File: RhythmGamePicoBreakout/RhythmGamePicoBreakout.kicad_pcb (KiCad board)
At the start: 2 copper layers, 80 x 54 mm, 71 parts, among them J1 BUTTON0, J10 BUTTON9, J11 BUTTON10, J12 QE1, J13 QE2, J14 Conn_01x02_Pin, J15 RGB1, J16 RGB2, J17 USB Header, J18 USB_C_Receptacle_USB2.0, J19 Conn_01x03, J2 BUTTON1, J20 PS2 Header, J21 Conn_01x02_Pin, J3 BUTTON2, J4 BUTTON3, J5 BUTTON4, J6 BUTTON5, J7 BUTTON6, J8 BUTTON7, J9 BUTTON8, Q1 LSI1012LT1G, Q10 LSI1012LT1G, Q11 LSI1012LT1G, Q2 LSI1012LT1G, Q3 LSI1012LT1G, Q4 LSI1012LT1G, Q5 LSI1012LT1G, Q6 LSI1012LT1G, Q7 LSI1012LT1G, Q8 LSI1012LT1G, Q9 LSI1012LT1G, U1 RP2040, U2 SRV05-4, U3 W25Q128JVS, U4 XC6206PxxxMR, U5 SN74HCT125D, U6 LM7805_TO220, Y1 Crystal_GND24

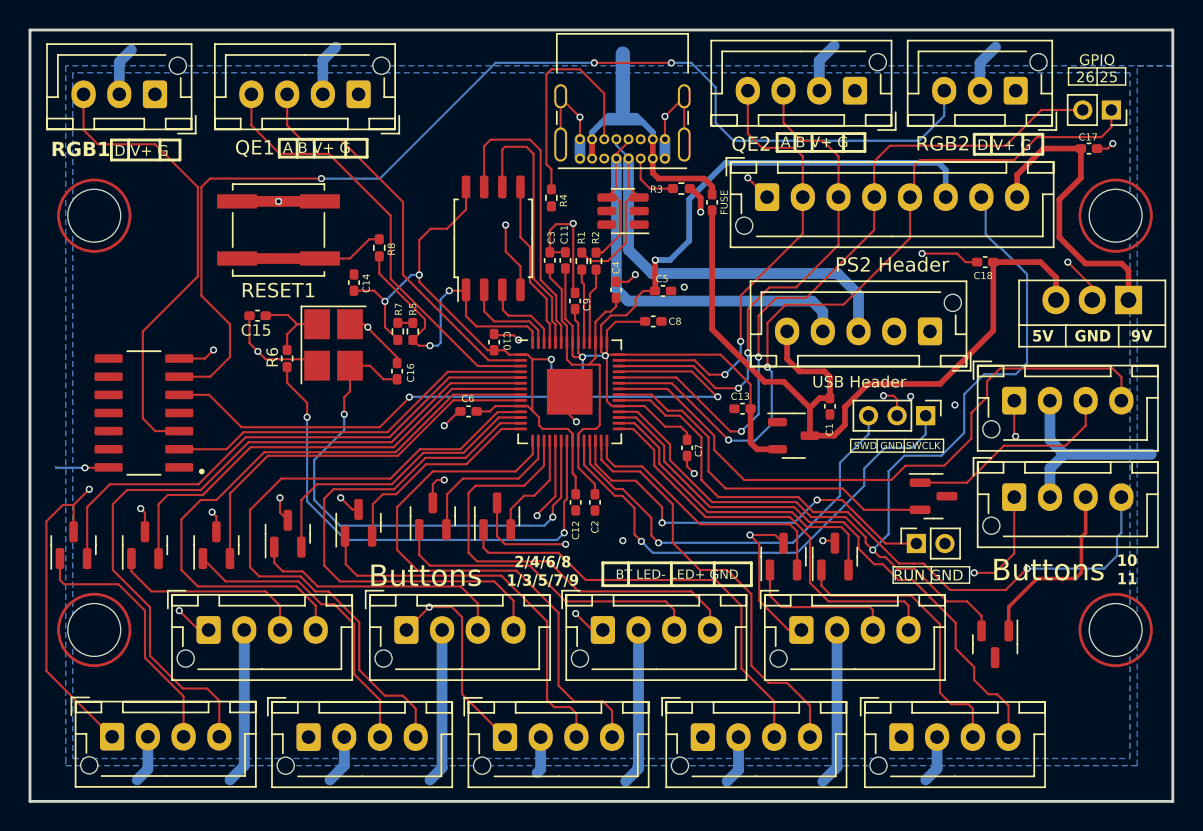
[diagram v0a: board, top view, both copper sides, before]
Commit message: Updated schematics and completely redone tracing
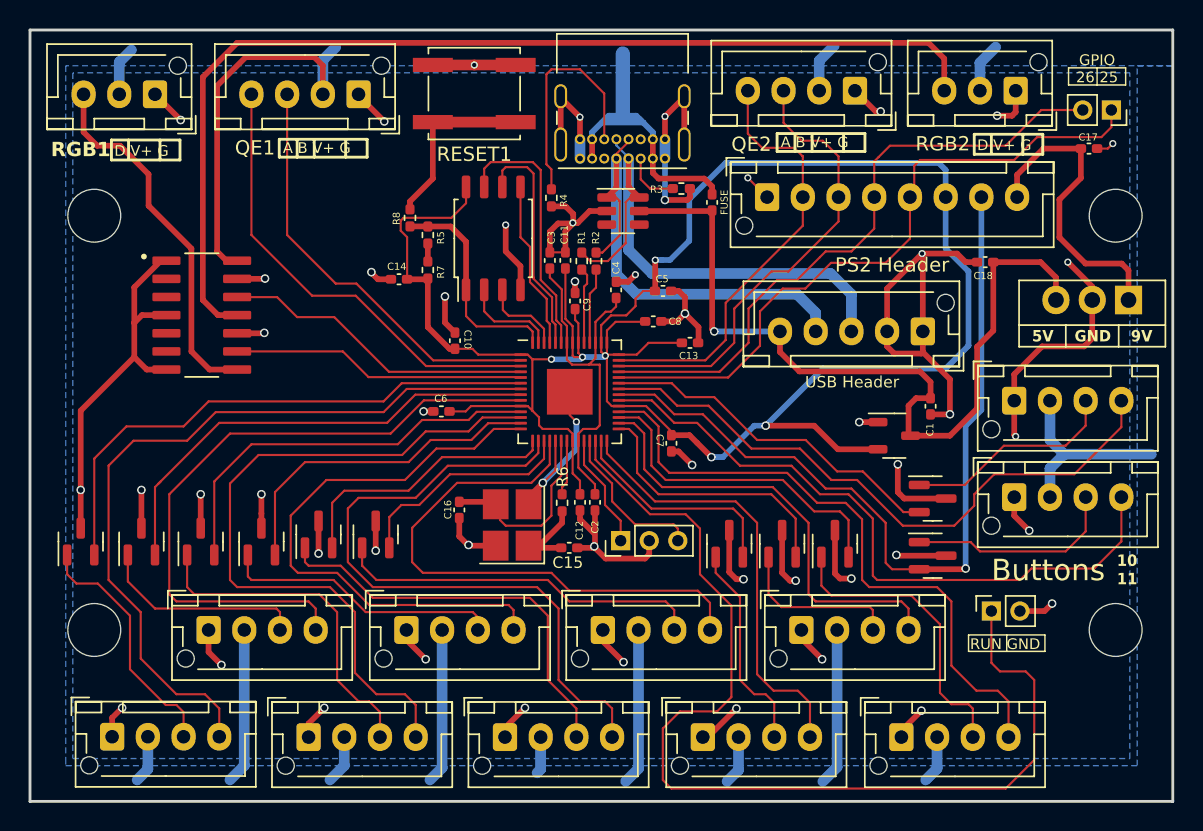
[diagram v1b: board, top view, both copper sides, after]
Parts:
- J19: value Conn_01x03 -> DEBUG
- moved C15 27.2 mm to (103.2, 161.8), turned to 180 degrees
- moved J19 23.1 mm to (106.8, 161.2), turned to 90 degrees
- moved R6 21.7 mm to (102.8, 158.6), turned to 90 degrees
- moved Y1 17.7 mm to (99.2, 160.2), turned to 90 degrees
- moved RESET1 16.7 mm to (96.6, 129.9)
- moved Q7 16.4 mm to (114.5, 161.5)
- moved C16 10.6 mm to (95.5, 159.1), turned to 90 degrees
- moved U5 7.96 mm to (77.5, 145.5), turned to 0 degrees
- moved Q11 7.59 mm to (128.7, 162.3), turned to 0 degrees
- moved J21 7.06 mm to (132.8, 166.2)
- moved C1 7.04 mm to (128.5, 151.8)
- moved U4 7.04 mm to (126.0, 153.9)
- moved R5 6.83 mm to (93.3, 139.9), turned to 90 degrees
- moved C13 5.90 mm to (111.7, 147.4), turned to 0 degrees
- moved R7 4.78 mm to (93.3, 142.3)
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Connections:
- U1 pad 11: /BT2 -> /LED2
- U1 pad 12: /LED3 -> /BT2
- U1 pad 13: /BT3 -> /LED3
- U1 pad 14: /LED4 -> /BT3
- U1 pad 15: /BT4 -> /LED4
- U1 pad 16: /LED5 -> /BT4
- U1 pad 17: /BT5 -> /LED5
- U1 pad 18: /LED6 -> /BT5
- U1 pad 27: /BT6 -> /LED6
- U1 pad 28: /LED7 -> /BT6
- U1 pad 29: /BT7 -> /LED7
- U1 pad 30: /LED8 -> /BT7
- U1 pad 31: /BT8 -> /LED8
- U1 pad 32: /LED10 -> /BT8
- U1 pad 35: /LED9 -> /LED10
- U1 pad 37: /GP25 -> /LED9
- U1 pad 38: /GP26 -> /GP25
- U1 pad 39: /RGBIn2 -> /GP26
- U1 pad 4: /RGBIn1 -> /RGBIn2
- U1 pad 5: /LED0 -> /RGBIn1
- U1 pad 6: /BT0 -> /LED0
- U1 pad 7: /LED1 -> /BT0
- U1 pad 8: /BT1 -> /LED1
- U1 pad 9: /LED2 -> /BT1
- U2 pad 1: unconnected-(U2-IO1-Pad1) -> USB_DM
- U2 pad 3: USB_DP -> unconnected-(U2-IO2-Pad3)
- U2 pad 4: USB_DM -> unconnected-(U2-IO3-Pad4)
- U2 pad 6: unconnected-(U2-IO4-Pad6) -> USB_DP
- U5 pad 11: unconnected-(U5-4Y-Pad11) -> /RGB2
- U5 pad 12: unconnected-(U5-4A-Pad12) -> /RGBIn2
- U5 pad 2: /RGBIn1 -> unconnected-(U5-1A-Pad2)
- U5 pad 3: /RGB1 -> unconnected-(U5-1Y-Pad3)
- U5 pad 5: /RGBIn2 -> unconnected-(U5-2A-Pad5)
- U5 pad 6: /RGB2 -> unconnected-(U5-2Y-Pad6)
- U5 pad 8: unconnected-(U5-3Y-Pad8) -> /RGB1
- U5 pad 9: unconnected-(U5-3A-Pad9) -> /RGBIn1
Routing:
- net GND: track 162.2 -> 244.5 mm, vias 38 -> 52
- net RUN: track 28.4 -> 72.5 mm, vias 2 -> 0
- net XOUT: track 35.8 -> 3.88 mm, vias 2 -> 0
- net +3V3: track 130.1 -> 157.5 mm
- net SWCLK: track 34.7 -> 8.05 mm, vias 1 -> 0
- net /RGBIn2: track 47.1 -> 22.0 mm, vias 2 -> 0
- net XIN: track 37.4 -> 13.8 mm, vias 2 -> 0
- net VBUS: track 116.9 -> 136.9 mm, vias 1 -> 0
- net SWD: track 29.9 -> 11.1 mm, vias 1 -> 0
- net Net-(J7-Pin_3): track 31.2 -> 14.8 mm
- net /LED10: track 66.5 -> 57.5 mm
- net /LED6: track 7.75 -> 15.6 mm
- net /BT4: track 39.5 -> 47.2 mm
- net /BT5: track 32.0 -> 39.5 mm
- net Q_SEL: track 22.6 -> 15.5 mm, vias 2 -> 0
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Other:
- board text added: "Designed by DJ Shoko"
- board text removed: "2/4/6/8 1/3/5/7/9"
